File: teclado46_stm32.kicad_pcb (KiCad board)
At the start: 2 copper layers, 232.7 x 80.3 mm, 153 parts, among them J1 78171-0004, U1 XC6206PxxxMR, U2 STM32G0B1CBTx

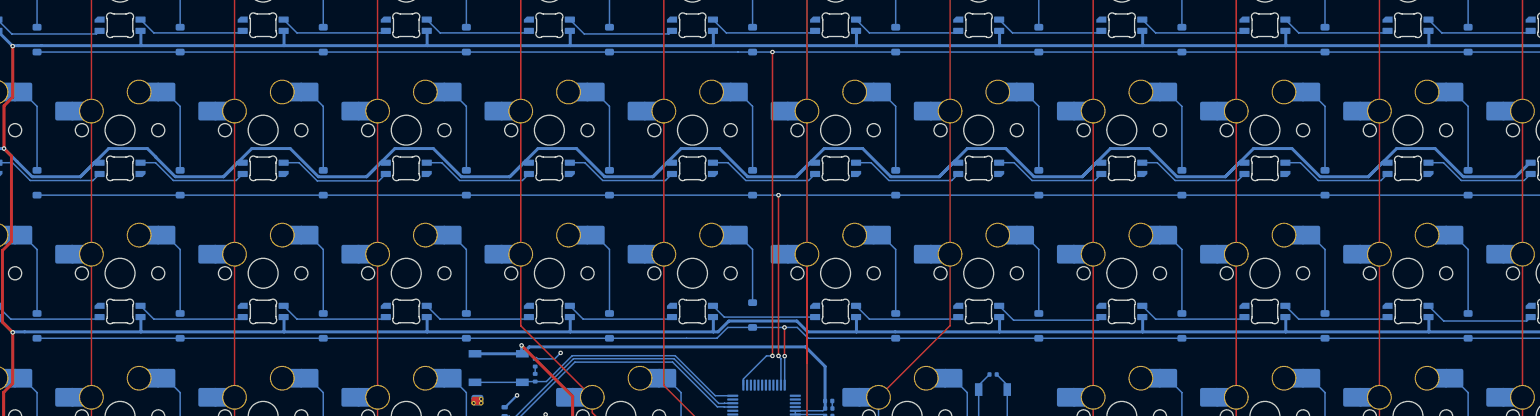
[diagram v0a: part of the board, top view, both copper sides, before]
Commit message: chore: add mounting holes
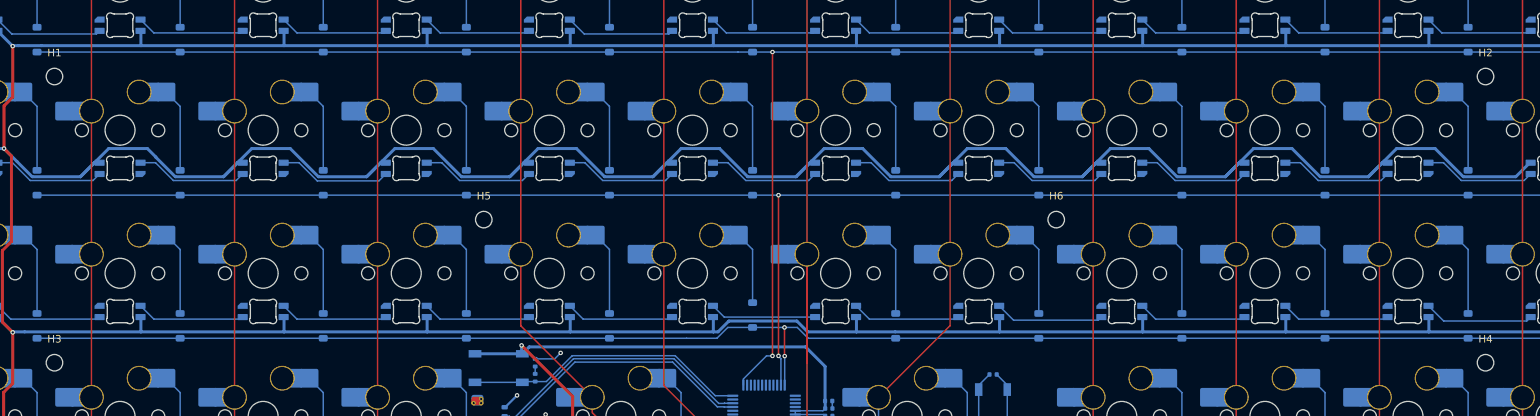
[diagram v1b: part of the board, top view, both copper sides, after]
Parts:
- added H1: MountingHole, MountingHole:MountingHole_2.2mm_M2, F.Cu at (48.4, 50.0)
- added H2: MountingHole, MountingHole:MountingHole_2.2mm_M2, F.Cu at (238.9, 50.0)
- added H3: MountingHole, MountingHole:MountingHole_2.2mm_M2, F.Cu at (48.4, 88.1)
- added H4: MountingHole, MountingHole:MountingHole_2.2mm_M2, F.Cu at (238.9, 88.1)
- added H5: MountingHole, MountingHole:MountingHole_2.2mm_M2, F.Cu at (105.6, 69.1)
- added H6: MountingHole, MountingHole:MountingHole_2.2mm_M2, F.Cu at (181.8, 69.1)

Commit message: chore: add lifting holes
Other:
- board size 232.7 x 80.3 mm -> 232.6 x 80.6 mm
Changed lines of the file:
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@@
 	)
 	(gr_line
-		(start 27.42138 26.829482)
-		(end 28.156464 26.525)
+		(start 26.59063 87.709375)
+		(end 26.590626 104.156249)
 		(stroke
-			(width 0.4)
+			(width 0.05)
 			(type default)
 		)
@@
 	)
 	(gr_line
-		(start 28.156464 106.825)
-		(end 27.42138 106.520518)
+		(start 240.109375 26.590625)
+		(end 256.159375 26.590625)
 		(stroke
-			(width 0.4)
+			(width 0.05)
+			(type default)
+		)
+		(layer "Edge.Cuts")
+	)
+	(gr_arc
+		(start 144.859375 26.590625)
+		(mid 142.875 28.575)
+		(end 140.890625 26.590625)
+		(stroke
+			(width 0.05)
+			(type solid)
+		)
+		(layer "Edge.Cuts")
+	)
+	(gr_arc
+		(start 26.590625 29.590625)
+		(mid 27.469297 27.469297)
+		(end 29.590625 26.590625)
+		(stroke
+			(width 0.05)
 			(type default)
 		)
@@
 	)
 	(gr_line
-		(start 28.156464 26.525)
-		(end 257.593536 26.525)
+		(start 144.859375 26.590625)
+		(end 236.140625 26.590625)
 		(stroke
-			(width 0.4)
+			(width 0.05)
 			(type default)
 		)
@@
 	)
 	(gr_line
-		(start 26.525 105.193536)
-		(end 26.525 28.156464)
+		(start 256.159375 107.15625)
+		(end 29.590626 107.15625)
 		(stroke
-			(width 0.4)
+			(width 0.05)
+			(type default)
+		)
+		(layer "Edge.Cuts")
+	)
+	(gr_arc
+		(start 26.590625 83.740625)
+		(mid 28.575 85.725)
+		(end 26.590625 87.709375)
+		(stroke
+			(width 0.05)
+			(type solid)
+		)
+		(layer "Edge.Cuts")
+	)
+	(gr_line
+		(start 26.59063 49.609375)
+		(end 26.59063 83.740625)
+		(stroke
+			(width 0.05)
+			(type default)
+		)
+		(layer "Edge.Cuts")
+	)
+	(gr_arc
+		(start 259.159375 104.15625)
+		(mid 258.280695 106.27757)
+		(end 256.159375 107.15625)
+		(stroke
+			(width 0.05)
 			(type default)
 		)
@@
 	)
 	(gr_line
-		(start 26.525 28.156464)
-		(end 26.829482 27.42138)
+		(start 259.159375 104.15625)
+		(end 259.159375 29.590625)
 		(stroke
-			(width 0.4)
+			(width 0.05)
+			(type default)
+		)
+		(layer "Edge.Cuts")
+	)
+	(gr_arc
+		(start 256.159375 26.590625)
+		(mid 258.280703 27.469297)
+		(end 259.159375 29.590625)
+		(stroke
+			(width 0.05)
 			(type default)
 		)
@@
 	)
 	(gr_line
-		(start 258.920518 27.42138)
-		(end 259.225 28.156464)
+		(start 26.590625 45.640625)
+		(end 26.590625 29.590625)
 		(stroke
-			(width 0.4)
+			(width 0.05)
+			(type default)
+		)
+		(layer "Edge.Cuts")
+	)
+	(gr_arc
+		(start 29.590626 107.15625)
+		(mid 27.469308 106.277569)
+		(end 26.590626 104.156249)
+		(stroke
+			(width 0.05)
 			(type default)
 		)
@@
 	)
 	(gr_line
-		(start 259.225 105.193536)
-		(end 258.920518 105.92862)
+		(start 45.640625 26.590625)
+		(end 29.590625 26.590625)
 		(stroke
-			(width 0.4)
+			(width 0.05)
 			(type default)
 		)
 		(layer "Edge.Cuts")
 	)
+	(gr_arc
+		(start 26.590625 45.640625)
+		(mid 28.575 47.625)
+		(end 26.590625 49.609375)
+		(stroke
+			(width 0.05)
+			(type solid)
+		)
+		(layer "Edge.Cuts")
+	)
 	(gr_line
-		(start 27.42138 106.520518)
-		(end 26.829482 105.92862)
+		(start 49.609375 26.590625)
+		(end 140.890625 26.590625)
 		(stroke
-			(width 0.4)
+			(width 0.05)
 			(type default)
 		)
 		(layer "Edge.Cuts")
 	)
-	(gr_line
-		(start 258.32862 106.520518)
-		(end 257.593536 106.825)
+	(gr_arc
+		(start 49.609375 26.590625)
+		(mid 47.625 28.575)
+		(end 45.640625 26.590625)
 		(stroke
-			(width 0.4)
-			(type default)
+			(width 0.05)
+			(type solid)
 		)
 		(layer "Edge.Cuts")
 	)
-	(gr_line
-		(start 26.829482 105.92862)
-		(end 26.525 105.193536)
+	(gr_arc
+		(start 240.109375 26.590625)
+		(mid 238.125 28.575)
+		(end 236.140625 26.590625)
 		(stroke
-			(width 0.4)
-			(type default)
+			(width 0.05)
+			(type solid)
 		)
 		(layer "Edge.Cuts")
-	)
-	(gr_line
-		(start 259.225 28.156464)
-		(end 259.225 105.193536)
-		(stroke
-			(width 0.4)
-			(type default)
-		)
-		(layer "Edge.Cuts")
-	)
-	(gr_line
-		(start 26.829482 27.42138)
-		(end 27.42138 26.829482)
-		(stroke
-			(width 0.4)
-			(type default)
-		)
-		(layer "Edge.Cuts")
-	)
-	(gr_line
-		(start 257.593536 26.525)
-		(end 258.32862 26.829482)
-		(stroke
-			(width 0.4)
-			(type default)
-		)
-		(layer "Edge.Cuts")
-	)
-	(gr_line
-		(start 257.593536 106.825)
-		(end 28.156464 106.825)
-		(stroke
-			(width 0.4)
-			(type default)
-		)
-		(layer "Edge.Cuts")
-	)
-	(gr_line
-		(start 258.920518 105.92862)
-		(end 258.32862 106.520518)
-		(stroke
-			(width 0.4)
-			(type default)
-		)
-		(layer "Edge.Cuts")
-	)
-	(gr_line
-		(start 258.32862 26.829482)
-		(end 258.920518 27.42138)
-		(stroke
-			(width 0.4)
-			(type default)
-		)
-		(layer "Edge.Cuts")

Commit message: chore: removed redundant fill zone
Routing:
- removed copper zone on F.Cu, net +3V3
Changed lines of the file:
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@@
-	)
-	(zone
-		(net 5)
-		(net_name "+3V3")
-		(layer "F.Cu")
-		(hatch edge 0.5)
-		(connect_pads
-			(clearance 0.4)
-		)
-		(min_thickness 0.25)
-		(filled_areas_thickness no)
-		(fill yes
-			(mode hatch)
-			(thermal_gap 0.5)
-			(thermal_bridge_width 0.5)
-			(island_removal_mode 1)
-			(island_area_min 10)
-			(hatch_thickness 1.5)
-			(hatch_gap 2.5)
-			(hatch_orientation 45)
-			(hatch_border_algorithm hatch_thickness)
-			(hatch_min_hole_area 0.3)
-		)
-		(polygon
-			(pts
-				(xy 268.2875 117.871875) (xy 19.84375 117.871875) (xy 20.6375 207.565625) (xy 267.49375 207.565625)
-			)
-		)
 	)
 	(zone
